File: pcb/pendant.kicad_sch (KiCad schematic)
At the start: 246 parts, among them J1 Conn_01x02, J2 USB_B_Micro, U1 ATSAMD21G18A-A, U2 LSM6DS3, U3 XC6206PxxxMR, U4 TP4057

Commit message: Revise PCB
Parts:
- added TP36, TP37, TP38, TP39, TP40: TestPoint, TestPoint:TestPoint_THTPad_D2.0mm_Drill1.0mm, symbol Connector:TestPoint
- added TP41, TP42, TP43, TP44, TP45: TestPoint, TestPoint:TestPoint_Pad_D3.0mm, symbol Connector:TestPoint
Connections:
- net +3V3: now also TP36.1, TP41.1
- net GND: now also TP37.1, TP42.1
- net RESET: now also TP38.1, TP43.1
- net SWCLK: now also TP39.1, TP44.1
- net SWDIO: now also TP40.1, TP45.1

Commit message: Format schematic
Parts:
- D1, D10, D100, D101, D102, D103, D104, D105, D106, D107, D108, D109, D11, D110, D111, D112, D113, D114, D115, D116, D117, D118, D119, D12, D120, D121, D122, D123, D124, D125, D126, D127, D128, D129, D13, D130, D131, D132, D133, D134, D135, D136, D137, D138, D139, D14, D140, D141, D142, D143, D144, D145, D146, D147, D148, D149, D15, D150, D151, D152, D153, D154, D155, D156, D157, D158, D159, D16, D160, D161, D162, D163, D164, D165, D166, D167, D168, D169, D17, D170, D171, D172, D18, D19, D2, D20, D21, D22, D23, D24, D25, D26, D27, D28, D29, D3, D30, D31, D32, D33, D34, D35, D36, D37, D38, D39, D4, D40, D41, D42, D43, D44, D45, D46, D47, D48, D49, D5, D50, D51, D52, D53, D54, D55, D56, D57, D58, D59, D6, D60, D61, D62, D63, D64, D65, D66, D67, D68, D69, D7, D70, D71, D72, D73, D74, D75, D76, D77, D78, D79, D8, D80, D81, D82, D83, D84, D85, D86, D87, D88, D89, D9, D90, D91, D92, D93, D94, D95, D96, D97, D98, D99: symbol Device:LED_Small -> Project:LED_Small
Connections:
- net +3V3: now also C10.1, R23.1; no longer C10.2, R23.2
- net +BATT: now also C4.2; no longer C4.1
- net GND: now also C10.2, C11.2, C3.1, C4.1; no longer C10.1, C11.1, C3.2, C4.2
- net STDBY: now also R23.2; no longer R23.1
- net VBUS: now also C11.1, C3.2; no longer C11.2, C3.1
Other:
- moved on the sheet: C1, C10, C11, C2, C3, C4, C5, C6, C7, C8, C9, J1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

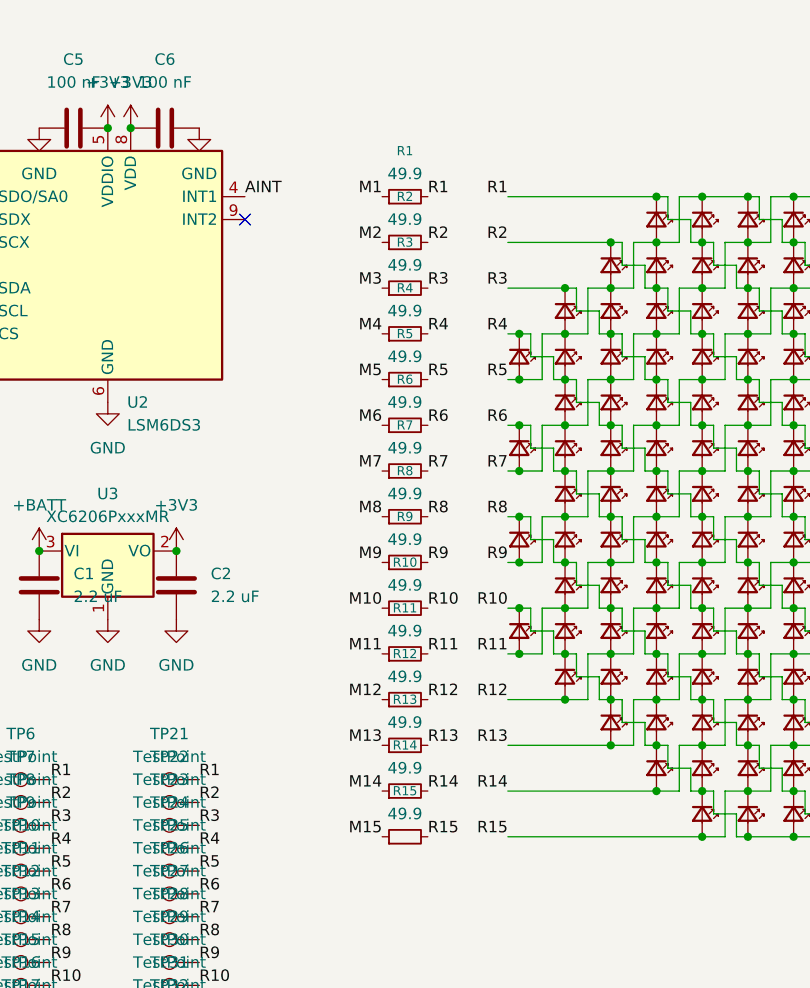
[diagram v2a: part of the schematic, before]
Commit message: Update LEDs
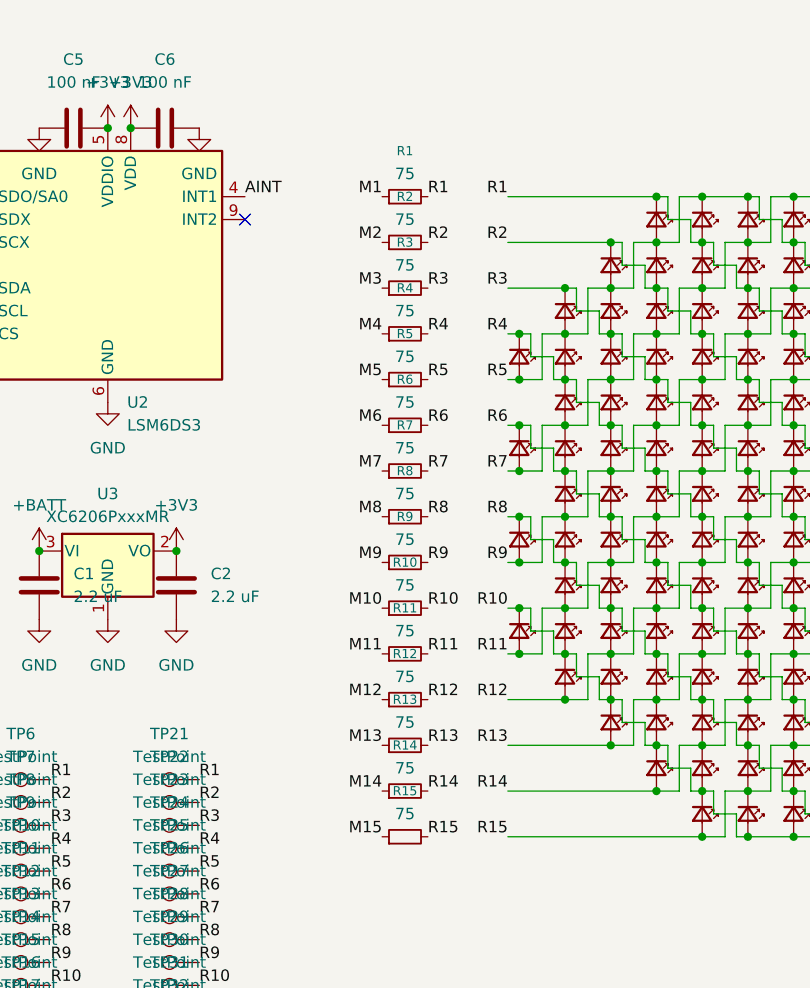
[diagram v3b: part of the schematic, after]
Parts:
- R1, R10, R11, R12, R13, R14, R15, R2, R3, R4, R5, R6, R7, R8, R9: value 49.9 -> 75
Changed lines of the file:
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@@
 			)
 		)
-		(property "Value" "49.9"
+		(property "Value" "75"
 			(at 191.77 76.2 90)
 			(show_name no)
@@
 			)
 		)
-		(property "Value" "49.9"
+		(property "Value" "75"
 			(at 191.77 91.44 90)
 			(show_name no)
@@
 			)
 		)
-		(property "Value" "49.9"
+		(property "Value" "75"
 			(at 191.77 96.52 90)
 			(show_name no)
@@
 			)
 		)
-		(property "Value" "49.9"
+		(property "Value" "75"
 			(at 191.77 81.28 90)
 			(show_name no)
@@
 			)
 		)
-		(property "Value" "49.9"
+		(property "Value" "75"
 			(at 191.77 55.88 90)
 			(show_name no)
@@
 			)
 		)
-		(property "Value" "49.9"
+		(property "Value" "75"
 			(at 191.77 86.36 90)
 			(show_name no)
@@
 			)
 		)
-		(property "Value" "49.9"
+		(property "Value" "75"
 			(at 191.77 71.12 90)
 			(show_name no)
@@
 			)
 		)
-		(property "Value" "49.9"
+		(property "Value" "75"
 			(at 191.77 60.96 90)
 			(show_name no)
@@
 			)
 		)
-		(property "Value" "49.9"
+		(property "Value" "75"
 			(at 191.77 106.68 90)
 			(show_name no)
@@
 			)
 		)
-		(property "Value" "49.9"
+		(property "Value" "75"
 			(at 191.77 66.04 90)
 			(show_name no)
@@
 			)
 		)
-		(property "Value" "49.9"
+		(property "Value" "75"
 			(at 191.77 50.8 90)
 			(show_name no)
@@
 			)
 		)
-		(property "Value" "49.9"
+		(property "Value" "75"
 			(at 191.77 116.84 90)
 			(show_name no)
@@
 			)
 		)
-		(property "Value" "49.9"
+		(property "Value" "75"
 			(at 191.77 111.76 90)
 			(show_name no)
@@
 			)
 		)
-		(property "Value" "49.9"
+		(property "Value" "75"
 			(at 191.77 101.6 90)
 			(show_name no)
@@
 			)
 		)
-		(property "Value" "49.9"
+		(property "Value" "75"
 			(at 191.77 45.72 90)
 			(show_name no)

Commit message: Check values
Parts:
- C1, C2: value 2.2 uF -> 1 uF
- R18, R19: value 4.7k -> 10k
- R21: value 15k -> 75k
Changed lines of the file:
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@@
 			)
 		)
-		(property "Value" "4.7k"
+		(property "Value" "10k"
 			(at 139.7 57.15 90)
 			(show_name no)
@@
 			)
 		)
-		(property "Value" "4.7k"
+		(property "Value" "10k"
 			(at 139.7 54.61 90)
 			(show_name no)
@@
 			)
 		)
-		(property "Value" "2.2 uF"
+		(property "Value" "1 uF"
 			(at 170.18 92.7099 0)
 			(show_name no)
@@
 			)
 		)
-		(property "Value" "2.2 uF"
+		(property "Value" "1 uF"
 			(at 154.94 92.7099 0)
 			(show_name no)
@@
 			)
 		)
-		(property "Value" "15k"
+		(property "Value" "75k"
 			(at 52.07 120.65 90)
 			(show_name no)

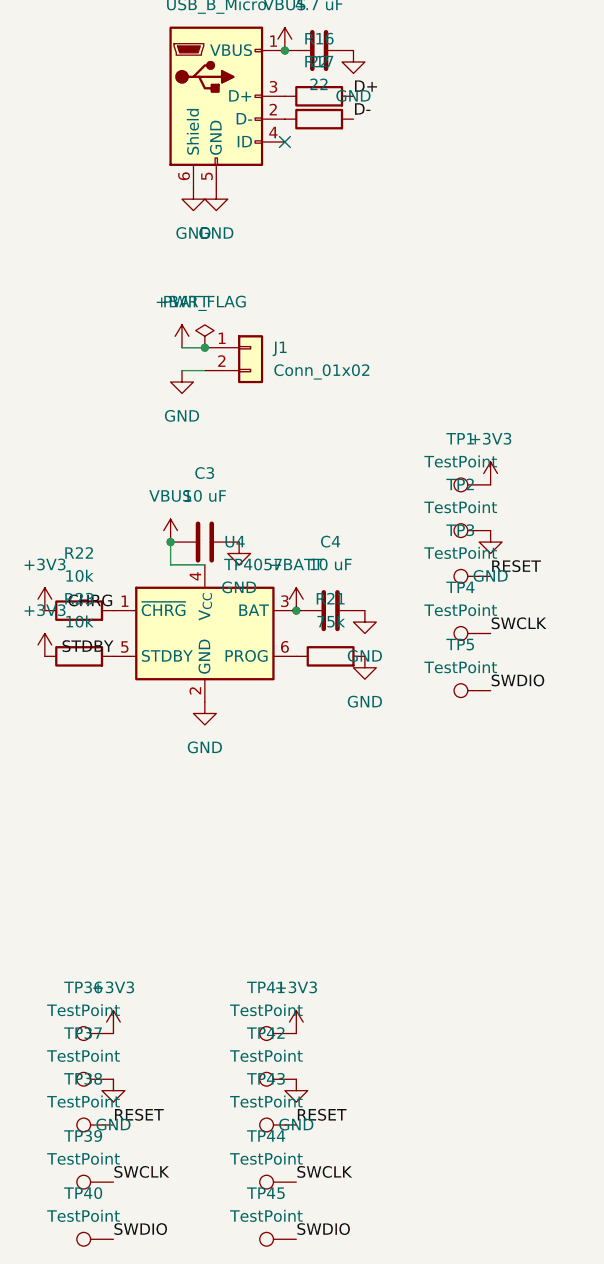
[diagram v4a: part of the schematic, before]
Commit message: Adjust SWD pad pitch
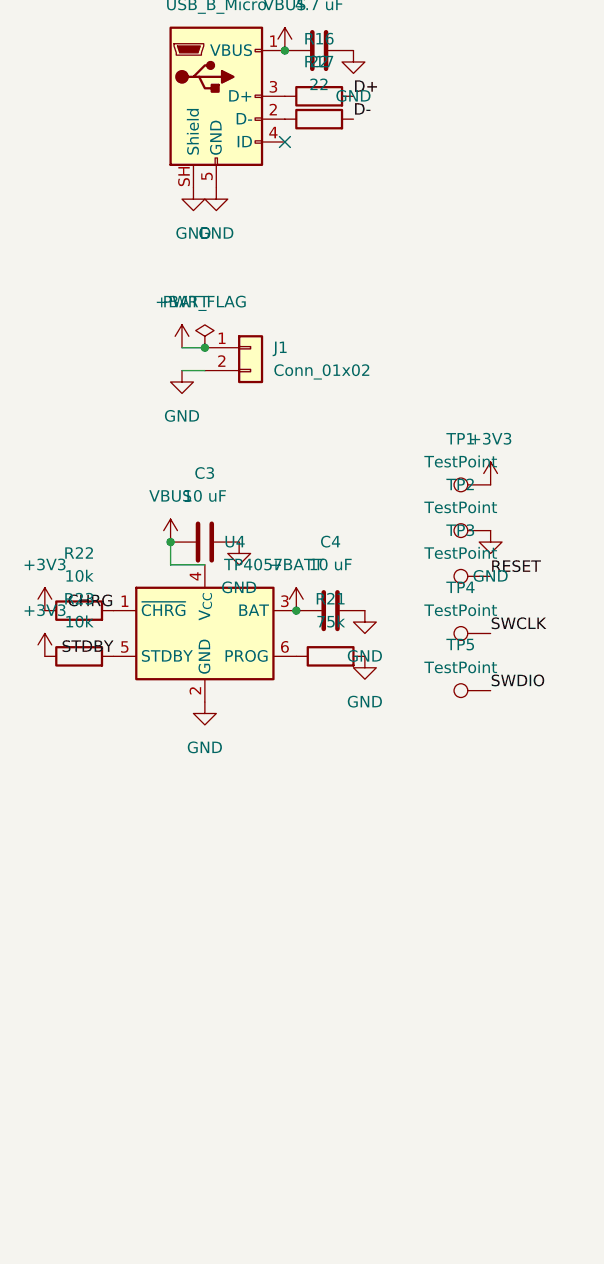
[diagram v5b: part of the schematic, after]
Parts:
- removed TP36, TP37, TP38, TP39, TP40: TestPoint, TestPoint:TestPoint_THTPad_D2.0mm_Drill1.0mm, symbol Connector:TestPoint
- removed TP41, TP42, TP43, TP44, TP45: TestPoint, TestPoint:TestPoint_Pad_D3.0mm, symbol Connector:TestPoint
- TP1, TP2, TP3, TP4, TP5: footprint TestPoint:TestPoint_Pad_D1.5mm -> Project:Pad_SMD_1.5x1.5
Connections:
- net GND: now also J2.SH (Shield); no longer J2.6 (Shield)
